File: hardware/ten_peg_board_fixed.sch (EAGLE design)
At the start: 121 parts, among them U1 ATTINY402, U10 ATTINY402, U2 ATTINY402, U3 ATTINY402, U4 ATTINY402, U5 ATTINY402, U6 ATTINY402, U7 ATTINY402, U8 ATTINY402, U9 ATTINY402

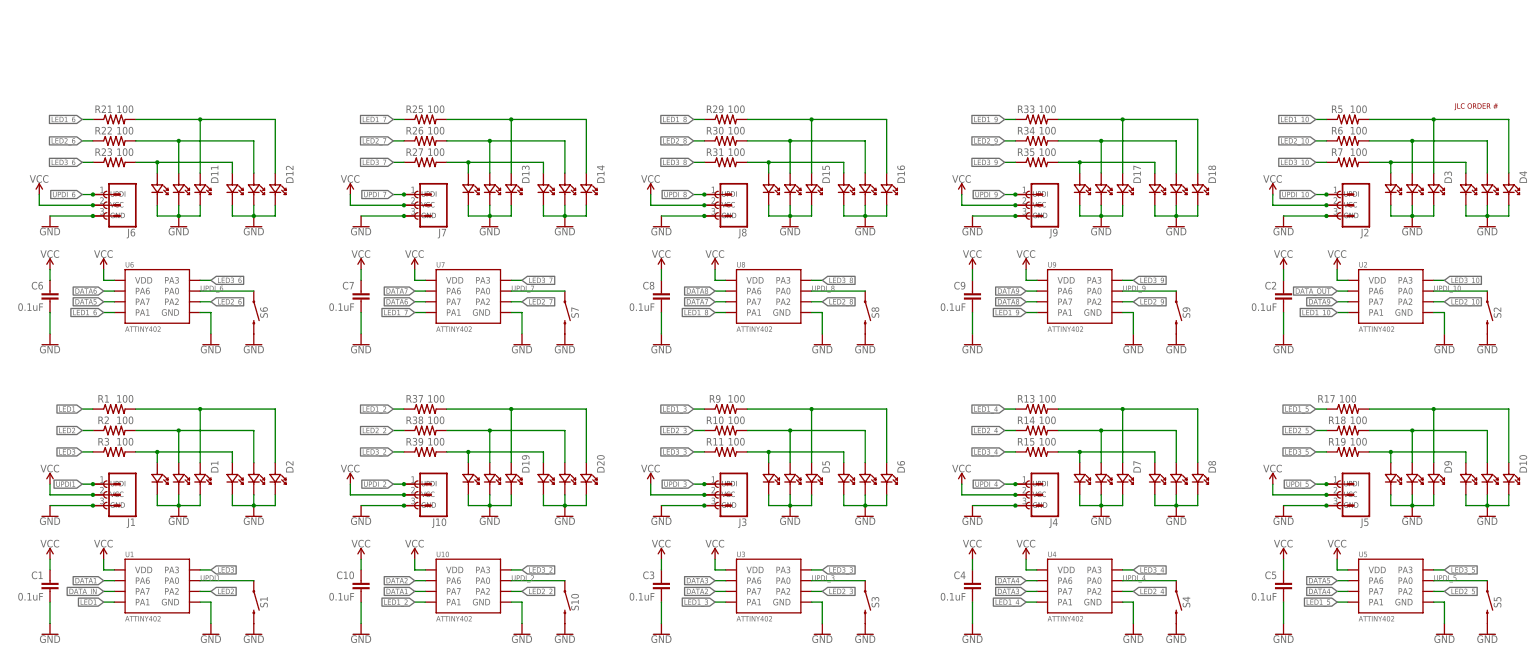
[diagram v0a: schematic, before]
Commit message: add color picker and add more comments
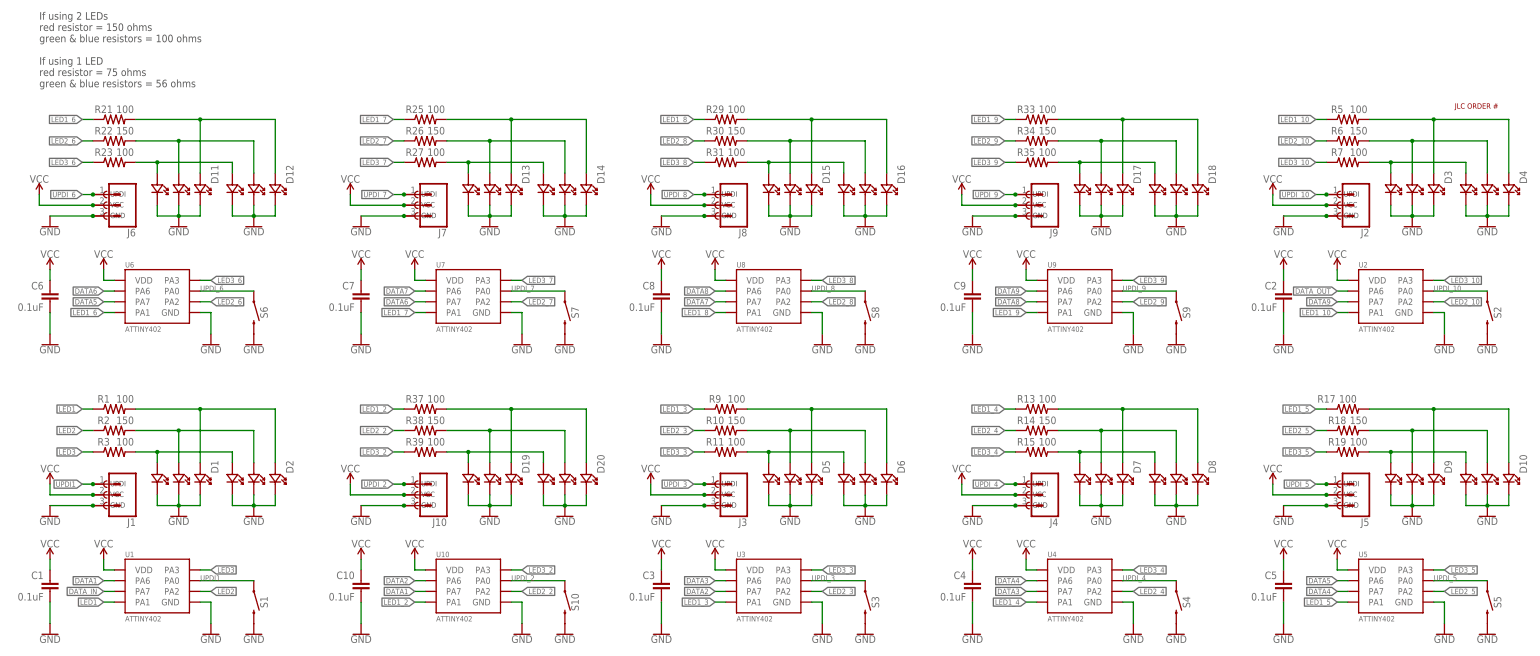
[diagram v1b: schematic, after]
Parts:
- R10, R14, R18, R2, R22, R26, R30, R34, R38, R6: value 100 -> 150
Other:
- note added: "If using 2 LEDs red resistor = 150 ohms green & blue resistors = 100 ohms If using 1 LED red resistor = 75 ohms green & blue resistors = 56 ohms"
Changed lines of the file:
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@@
 <part name="GND3" library="SparkFun-PowerSymbols" deviceset="GND" device=""/>
 <part name="R1" library="SparkFun-Resistors" deviceset="100OHM" device="-0603-1/4W-5%" value="100"/>
-<part name="R2" library="SparkFun-Resistors" deviceset="100OHM" device="-0603-1/4W-5%" value="100"/>
+<part name="R2" library="SparkFun-Resistors" deviceset="100OHM" device="-0603-1/4W-5%" value="150"/>
 <part name="R3" library="SparkFun-Resistors" deviceset="100OHM" device="-0603-1/4W-5%" value="100"/>
 <part name="D1" library="IDEO-Diodes" deviceset="19-337C/RSBHGHC-A88/4T" device=""/>
@@
 <part name="GND9" library="SparkFun-PowerSymbols" deviceset="GND" device=""/>
 <part name="R5" library="SparkFun-Resistors" deviceset="100OHM" device="-0603-1/4W-5%" value="100"/>
-<part name="R6" library="SparkFun-Resistors" deviceset="100OHM" device="-0603-1/4W-5%" value="100"/>
+<part name="R6" library="SparkFun-Resistors" deviceset="100OHM" device="-0603-1/4W-5%" value="150"/>
 <part name="R7" library="SparkFun-Resistors" deviceset="100OHM" device="-0603-1/4W-5%" value="100"/>
 <part name="D3" library="IDEO-Diodes" deviceset="19-337C/RSBHGHC-A88/4T" device=""/>
@@
 <part name="GND15" library="SparkFun-PowerSymbols" deviceset="GND" device=""/>
 <part name="R9" library="SparkFun-Resistors" deviceset="100OHM" device="-0603-1/4W-5%" value="100"/>
-<part name="R10" library="SparkFun-Resistors" deviceset="100OHM" device="-0603-1/4W-5%" value="100"/>
+<part name="R10" library="SparkFun-Resistors" deviceset="100OHM" device="-0603-1/4W-5%" value="150"/>
 <part name="R11" library="SparkFun-Resistors" deviceset="100OHM" device="-0603-1/4W-5%" value="100"/>
 <part name="D5" library="IDEO-Diodes" deviceset="19-337C/RSBHGHC-A88/4T" device=""/>
@@
 <part name="GND21" library="SparkFun-PowerSymbols" deviceset="GND" device=""/>
 <part name="R13" library="SparkFun-Resistors" deviceset="100OHM" device="-0603-1/4W-5%" value="100"/>
-<part name="R14" library="SparkFun-Resistors" deviceset="100OHM" device="-0603-1/4W-5%" value="100"/>
+<part name="R14" library="SparkFun-Resistors" deviceset="100OHM" device="-0603-1/4W-5%" value="150"/>
 <part name="R15" library="SparkFun-Resistors" deviceset="100OHM" device="-0603-1/4W-5%" value="100"/>
 <part name="D7" library="IDEO-Diodes" deviceset="19-337C/RSBHGHC-A88/4T" device=""/>
@@
 <part name="GND27" library="SparkFun-PowerSymbols" deviceset="GND" device=""/>
 <part name="R17" library="SparkFun-Resistors" deviceset="100OHM" device="-0603-1/4W-5%" value="100"/>
-<part name="R18" library="SparkFun-Resistors" deviceset="100OHM" device="-0603-1/4W-5%" value="100"/>
+<part name="R18" library="SparkFun-Resistors" deviceset="100OHM" device="-0603-1/4W-5%" value="150"/>
 <part name="R19" library="SparkFun-Resistors" deviceset="100OHM" device="-0603-1/4W-5%" value="100"/>
 <part name="D9" library="IDEO-Diodes" deviceset="19-337C/RSBHGHC-A88/4T" device=""/>
@@
 <part name="GND33" library="SparkFun-PowerSymbols" deviceset="GND" device=""/>
 <part name="R21" library="SparkFun-Resistors" deviceset="100OHM" device="-0603-1/4W-5%" value="100"/>
-<part name="R22" library="SparkFun-Resistors" deviceset="100OHM" device="-0603-1/4W-5%" value="100"/>
+<part name="R22" library="SparkFun-Resistors" deviceset="100OHM" device="-0603-1/4W-5%" value="150"/>
 <part name="R23" library="SparkFun-Resistors" deviceset="100OHM" device="-0603-1/4W-5%" value="100"/>
 <part name="D11" library="IDEO-Diodes" deviceset="19-337C/RSBHGHC-A88/4T" device=""/>
@@
 <part name="GND39" library="SparkFun-PowerSymbols" deviceset="GND" device=""/>
 <part name="R25" library="SparkFun-Resistors" deviceset="100OHM" device="-0603-1/4W-5%" value="100"/>
-<part name="R26" library="SparkFun-Resistors" deviceset="100OHM" device="-0603-1/4W-5%" value="100"/>
+<part name="R26" library="SparkFun-Resistors" deviceset="100OHM" device="-0603-1/4W-5%" value="150"/>
 <part name="R27" library="SparkFun-Resistors" deviceset="100OHM" device="-0603-1/4W-5%" value="100"/>
 <part name="D13" library="IDEO-Diodes" deviceset="19-337C/RSBHGHC-A88/4T" device=""/>
@@
 <part name="GND45" library="SparkFun-PowerSymbols" deviceset="GND" device=""/>
 <part name="R29" library="SparkFun-Resistors" deviceset="100OHM" device="-0603-1/4W-5%" value="100"/>
-<part name="R30" library="SparkFun-Resistors" deviceset="100OHM" device="-0603-1/4W-5%" value="100"/>
+<part name="R30" library="SparkFun-Resistors" deviceset="100OHM" device="-0603-1/4W-5%" value="150"/>
 <part name="R31" library="SparkFun-Resistors" deviceset="100OHM" device="-0603-1/4W-5%" value="100"/>
 <part name="D15" library="IDEO-Diodes" deviceset="19-337C/RSBHGHC-A88/4T" device=""/>
@@
 <part name="GND51" library="SparkFun-PowerSymbols" deviceset="GND" device=""/>
 <part name="R33" library="SparkFun-Resistors" deviceset="100OHM" device="-0603-1/4W-5%" value="100"/>
-<part name="R34" library="SparkFun-Resistors" deviceset="100OHM" device="-0603-1/4W-5%" value="100"/>
+<part name="R34" library="SparkFun-Resistors" deviceset="100OHM" device="-0603-1/4W-5%" value="150"/>
 <part name="R35" library="SparkFun-Resistors" deviceset="100OHM" device="-0603-1/4W-5%" value="100"/>
 <part name="D17" library="IDEO-Diodes" deviceset="19-337C/RSBHGHC-A88/4T" device=""/>
@@
 <part name="GND57" library="SparkFun-PowerSymbols" deviceset="GND" device=""/>
 <part name="R37" library="SparkFun-Resistors" deviceset="100OHM" device="-0603-1/4W-5%" value="100"/>
-<part name="R38" library="SparkFun-Resistors" deviceset="100OHM" device="-0603-1/4W-5%" value="100"/>
+<part name="R38" library="SparkFun-Resistors" deviceset="100OHM" device="-0603-1/4W-5%" value="150"/>
 <part name="R39" library="SparkFun-Resistors" deviceset="100OHM" device="-0603-1/4W-5%" value="100"/>
 <part name="D19" library="IDEO-Diodes" deviceset="19-337C/RSBHGHC-A88/4T" device=""/>
@@
 <text x="247.904" y="159.512" size="1.27" layer="97">VCC</text>
 <text x="247.904" y="156.972" size="1.27" layer="97">GND</text>
+<text x="12.7" y="187.96" size="1.778" layer="97">If using 2 LEDs
+red resistor = 150 ohms
+green &amp; blue resistors = 100 ohms
+If using 1 LED
+red resistor = 75 ohms
+green &amp; blue resistors = 56 ohms</text>
 </plain>
 <instances>
@@
 </schematic>
 </drawing>
+<compatibility>
+<note version="6.3" minversion="6.2.2" severity="warning">
+Since Version 6.2.2 text objects can contain more than one line,
+which will not be processed correctly with this version.
+</note>
+</compatibility>
 </eagle>
